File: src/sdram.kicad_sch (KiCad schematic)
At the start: 8 parts, among them U1 ECP5U_12_CABGA256, U10 W9825G6KH-6

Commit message: Rev 2
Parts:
- C30, C32: LCSC Part (none) -> C19702
- C31, C33, C34, C35: LCSC Part (none) -> C1525
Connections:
- net LED1: now reaches U1.C13 (PT60B/-)
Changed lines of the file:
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@@
 		)
 	)
+	(global_label "LED1"
+		(shape input)
+		(at 214.63 115.57 180)
+		(effects
+			(font
+				(size 1.27 1.27)
+			)
+			(justify right)
+		)
+		(property "Intersheetrefs" "${INTERSHEET_REFS}"
+			(at 214.63 115.57 0)
+			(effects
+				(font
+					(size 1.27 1.27)
+					(thickness 0.254)
+					(bold yes)
+				)
+				(hide yes)
+			)
+		)
+	)
 	(global_label "SDRAM_A1"
 		(shape input)
@@
 			)
 		)
-		(property "LCSC Part" ""
+		(property "LCSC Part" "C19702"
 			(at 222.25 36.83 0)
 			(effects
@@
 			)
 		)
-		(property "LCSC Part" ""
+		(property "LCSC Part" "C1525"
 			(at 133.35 35.56 0)
 			(effects
@@
 			)
 		)
-		(property "LCSC Part" ""
+		(property "LCSC Part" "C1525"
 			(at 48.26 113.03 0)
 			(effects
@@
 			)
 		)
-		(property "LCSC Part" ""
+		(property "LCSC Part" "C1525"
 			(at 233.68 36.83 0)
 			(effects
@@
 			)
 		)
-		(property "LCSC Part" ""
+		(property "LCSC Part" "C1525"
 			(at 246.38 36.83 0)
 			(effects
@@
 			)
 		)
-		(property "LCSC Part" ""
+		(property "LCSC Part" "C19702"
 			(at 121.92 35.56 0)
 			(effects

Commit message: Tidy project
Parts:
- C30, C32: JLCPCB Part # (none) -> C19702; LCSC Part C19702 -> (none)
- C31, C33, C34, C35: JLCPCB Part # (none) -> C1525; LCSC Part C1525 -> (none)
- U1: JLCPCB Part # (none) -> C1521614; LCSC Part C1521614 -> (none)
- U10: JLCPCB Part # (none) -> C62246; LCSC Part C62246 -> (none)
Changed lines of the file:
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@@
 			)
 		)
-		(property "LCSC Part" "C19702"
+		(property "JLCPCB Part #" "C19702"
 			(at 222.25 36.83 0)
 			(effects
@@
 					(size 1.27 1.27)
 				)
-				(hide yes)
 			)
 		)
@@
 			)
 		)
-		(property "LCSC Part" " C1521614"
+		(property "JLCPCB Part #" " C1521614"
 			(at 236.22 85.09 0)
 			(effects
@@
 					(size 1.27 1.27)
 				)
-				(hide yes)
 			)
 		)
@@
 			)
 		)
-		(property "LCSC Part" " C1521614"
+		(property "JLCPCB Part #" " C1521614"
 			(at 63.5 162.56 0)
 			(effects
@@
 					(size 1.27 1.27)
 				)
-				(hide yes)
 			)
 		)
@@
 			)
 		)
-		(property "LCSC Part" " C62246"
+		(property "JLCPCB Part #" " C62246"
 			(at 49.53 53.34 0)
 			(effects
@@
 					(size 1.27 1.27)
 				)
-				(hide yes)
 			)
 		)
@@
 			)
 		)
-		(property "LCSC Part" "C1525"
+		(property "JLCPCB Part #" "C1525"
 			(at 133.35 35.56 0)
 			(effects
@@
 					(size 1.27 1.27)
 				)
-				(hide yes)
 			)
 		)
@@
 			)
 		)
-		(property "LCSC Part" "C1525"
+		(property "JLCPCB Part #" "C1525"
 			(at 48.26 113.03 0)
 			(effects
@@
 					(size 1.27 1.27)
 				)
-				(hide yes)
 			)
 		)
@@
 			)
 		)
-		(property "LCSC Part" "C1525"
+		(property "JLCPCB Part #" "C1525"
 			(at 233.68 36.83 0)
 			(effects
@@
 					(size 1.27 1.27)
 				)
-				(hide yes)
 			)
 		)
@@
 			)
 		)
-		(property "LCSC Part" " C1521614"
+		(property "JLCPCB Part #" " C1521614"
 			(at 135.89 85.09 0)
 			(effects
@@
 					(size 1.27 1.27)
 				)
-				(hide yes)
 			)
 		)
@@
 			)
 		)
-		(property "LCSC Part" "C1525"
+		(property "JLCPCB Part #" "C1525"
 			(at 246.38 36.83 0)
 			(effects
@@
 					(size 1.27 1.27)
 				)
-				(hide yes)
 			)
 		)
@@
 			)
 		)
-		(property "LCSC Part" "C19702"
+		(property "JLCPCB Part #" "C19702"
 			(at 121.92 35.56 0)
 			(effects
@@
 					(size 1.27 1.27)
 				)
-				(hide yes)
-			)
-		)
+			)
+		)

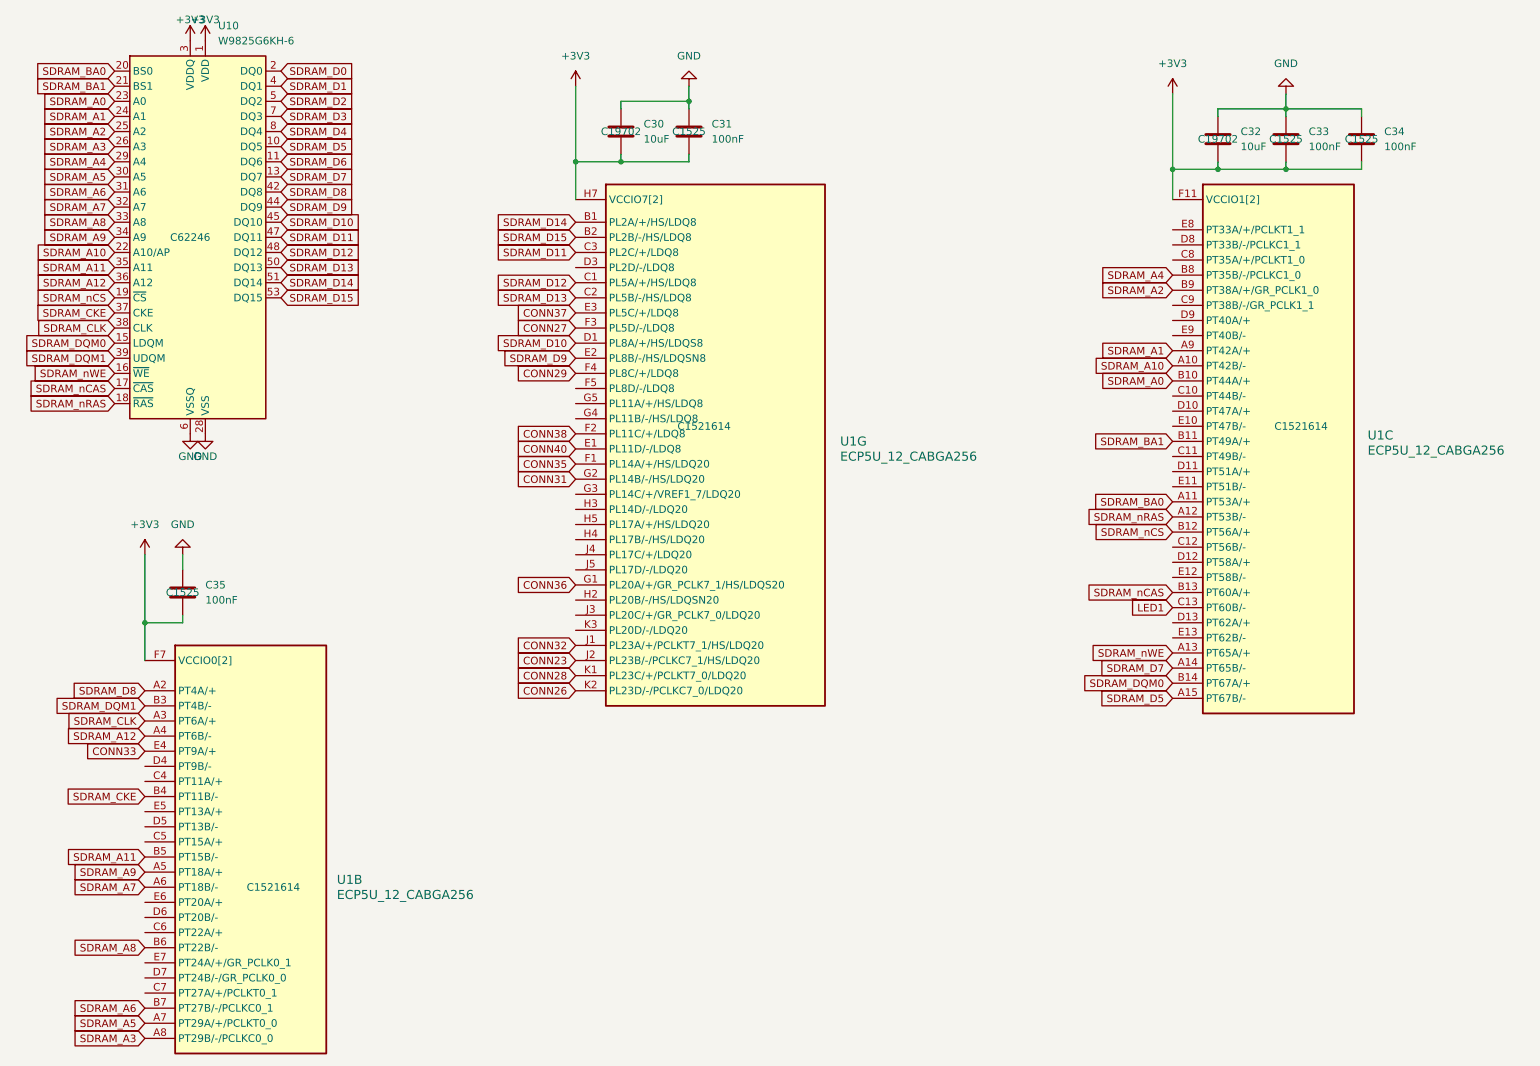
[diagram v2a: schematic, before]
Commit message: Add test points
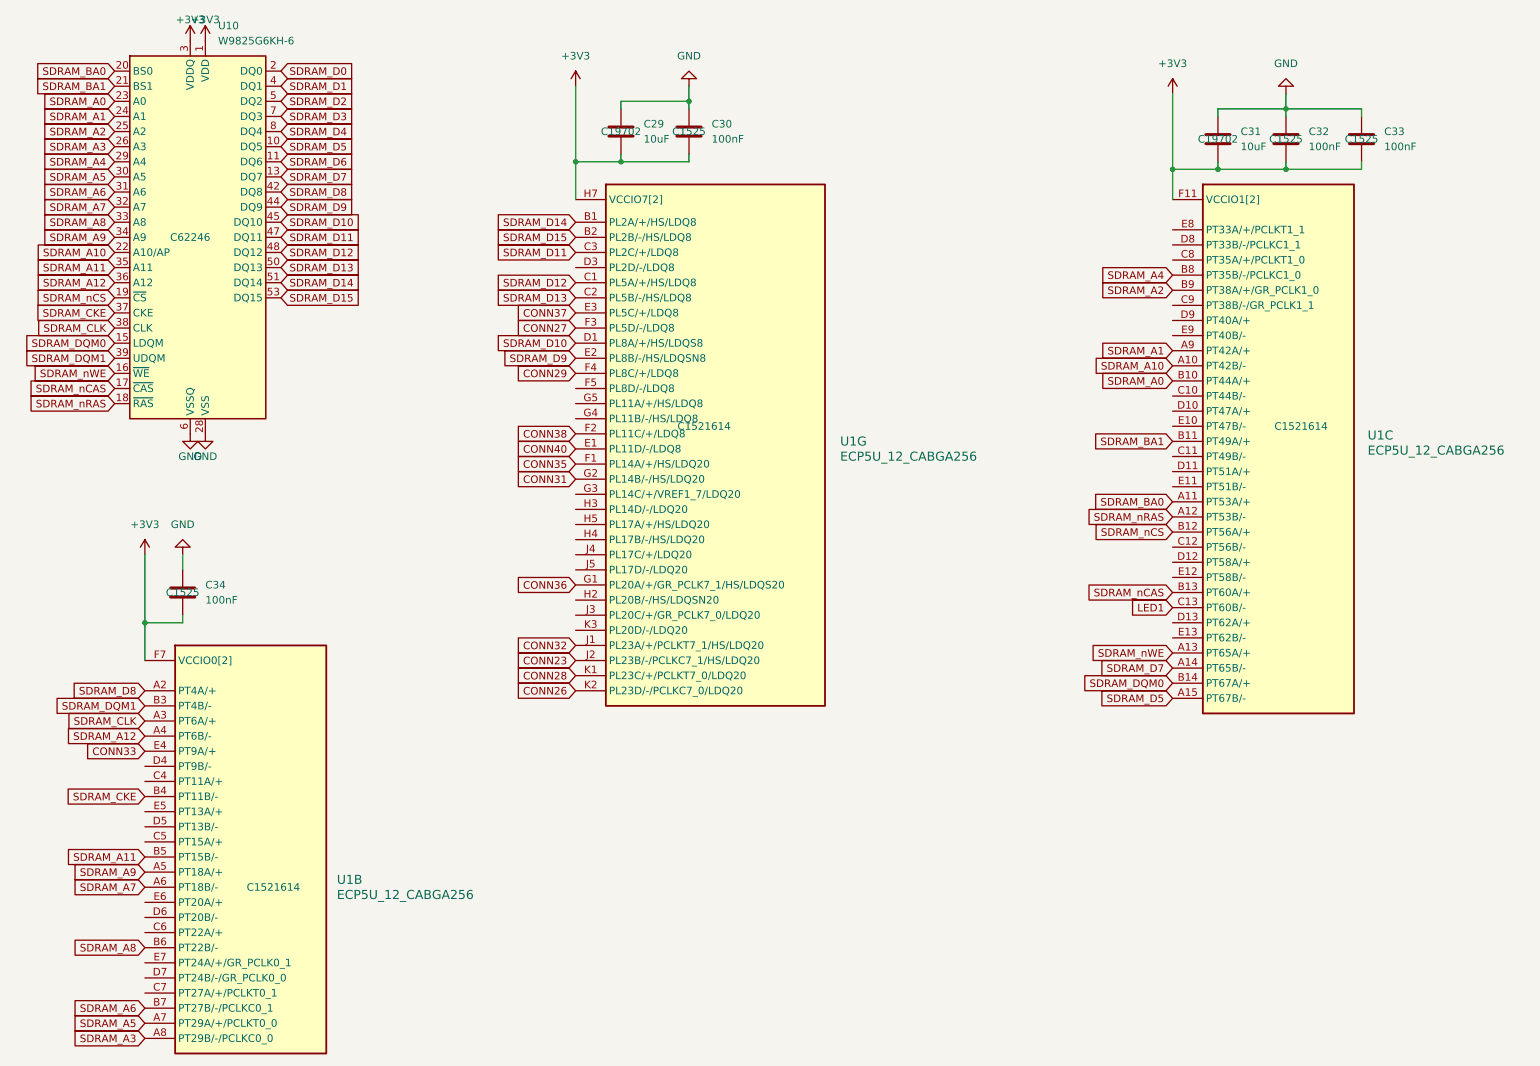
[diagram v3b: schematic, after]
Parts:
- renumbered C30 to C29, C31 to C30, C32 to C31, C33 to C32, C34 to C33, C35 to C34
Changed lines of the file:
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@@
 		(on_board yes)
 		(dnp no)
-		(property "Reference" "#PWR061"
+		(property "Reference" "#PWR070"
 			(at 49.53 24.13 0)
 			(effects
@@
 			(project "anice"
 				(path "/0f1188ca-7a22-47ac-a6b4-e14ae08f1e6d/b8864f4a-1b1e-4293-9ee7-0fecc8962eec"
-					(reference "#PWR061")
+					(reference "#PWR070")
 					(unit 1)
 				)
@@
 		(on_board yes)
 		(dnp no)
-		(property "Reference" "#PWR063"
+		(property "Reference" "#PWR076"
 			(at 49.53 92.71 0)
 			(effects
@@
 			(project "anice"
 				(path "/0f1188ca-7a22-47ac-a6b4-e14ae08f1e6d/b8864f4a-1b1e-4293-9ee7-0fecc8962eec"
-					(reference "#PWR063")
+					(reference "#PWR076")
 					(unit 1)
 				)
@@
 		(dnp no)
 		(fields_autoplaced yes)
-		(property "Reference" "C32"
+		(property "Reference" "C31"
 			(at 226.06 35.5599 0)
 			(effects
@@
 			(project "anice"
 				(path "/0f1188ca-7a22-47ac-a6b4-e14ae08f1e6d/b8864f4a-1b1e-4293-9ee7-0fecc8962eec"
-					(reference "C32")
+					(reference "C31")
 					(unit 1)
 				)
@@
 		(on_board yes)
 		(dnp no)
-		(property "Reference" "#PWR064"
+		(property "Reference" "#PWR077"
 			(at 52.07 92.71 0)
 			(effects
@@
 			(project "anice"
 				(path "/0f1188ca-7a22-47ac-a6b4-e14ae08f1e6d/b8864f4a-1b1e-4293-9ee7-0fecc8962eec"
-					(reference "#PWR064")
+					(reference "#PWR077")
 					(unit 1)
 				)
@@
 		(dnp no)
 		(fields_autoplaced yes)
-		(property "Reference" "C31"
+		(property "Reference" "C30"
 			(at 137.16 34.2899 0)
 			(effects
@@
 			(project "anice"
 				(path "/0f1188ca-7a22-47ac-a6b4-e14ae08f1e6d/b8864f4a-1b1e-4293-9ee7-0fecc8962eec"
-					(reference "C31")
+					(reference "C30")
 					(unit 1)
 				)
@@
 		(dnp no)
 		(fields_autoplaced yes)
-		(property "Reference" "#PWR083"
+		(property "Reference" "#PWR072"
 			(at 114.3 31.75 0)
 			(effects
@@
 			(project "anice"
 				(path "/0f1188ca-7a22-47ac-a6b4-e14ae08f1e6d/b8864f4a-1b1e-4293-9ee7-0fecc8962eec"
-					(reference "#PWR083")
+					(reference "#PWR072")
 					(unit 1)
 				)
@@
 		(dnp no)
 		(fields_autoplaced yes)
-		(property "Reference" "C35"
+		(property "Reference" "C34"
 			(at 52.07 111.7599 0)
 			(effects
@@
 			(project "anice"
 				(path "/0f1188ca-7a22-47ac-a6b4-e14ae08f1e6d/b8864f4a-1b1e-4293-9ee7-0fecc8962eec"
-					(reference "C35")
+					(reference "C34")
 					(unit 1)
 				)
@@
 		(dnp no)
 		(fields_autoplaced yes)
-		(property "Reference" "C33"
+		(property "Reference" "C32"
 			(at 237.49 35.5599 0)
 			(effects
@@
 			(project "anice"
 				(path "/0f1188ca-7a22-47ac-a6b4-e14ae08f1e6d/b8864f4a-1b1e-4293-9ee7-0fecc8962eec"
-					(reference "C33")
+					(reference "C32")
 					(unit 1)
 				)
@@
 		(dnp no)
 		(fields_autoplaced yes)
-		(property "Reference" "#PWR085"
+		(property "Reference" "#PWR074"
 			(at 214.63 33.02 0)
 			(effects
@@
 			(project "anice"
 				(path "/0f1188ca-7a22-47ac-a6b4-e14ae08f1e6d/b8864f4a-1b1e-4293-9ee7-0fecc8962eec"
-					(reference "#PWR085")
+					(reference "#PWR074")
 					(unit 1)
 				)
@@
 		(dnp no)
 		(fields_autoplaced yes)
-		(property "Reference" "#PWR088"
+		(property "Reference" "#PWR079"
 			(at 48.26 100.33 0)
 			(effects
@@
 			(project "anice"
 				(path "/0f1188ca-7a22-47ac-a6b4-e14ae08f1e6d/b8864f4a-1b1e-4293-9ee7-0fecc8962eec"
-					(reference "#PWR088")
+					(reference "#PWR079")
 					(unit 1)
 				)
@@
 		(dnp no)
 		(fields_autoplaced yes)
-		(property "Reference" "#PWR087"
+		(property "Reference" "#PWR078"
 			(at 41.91 110.49 0)
 			(effects
@@
 			(project "anice"
 				(path "/0f1188ca-7a22-47ac-a6b4-e14ae08f1e6d/b8864f4a-1b1e-4293-9ee7-0fecc8962eec"
-					(reference "#PWR087")
+					(reference "#PWR078")
 					(unit 1)
 				)
@@
 		(dnp no)
 		(fields_autoplaced yes)
-		(property "Reference" "C34"
+		(property "Reference" "C33"
 			(at 250.19 35.5599 0)
 			(effects
@@
 			(project "anice"
 				(path "/0f1188ca-7a22-47ac-a6b4-e14ae08f1e6d/b8864f4a-1b1e-4293-9ee7-0fecc8962eec"
-					(reference "C34")
+					(reference "C33")
 					(unit 1)
 				)
@@
 		(dnp no)
 		(fields_autoplaced yes)
-		(property "Reference" "#PWR084"
+		(property "Reference" "#PWR073"
 			(at 133.35 21.59 0)
 			(effects
@@
 			(project "anice"
 				(path "/0f1188ca-7a22-47ac-a6b4-e14ae08f1e6d/b8864f4a-1b1e-4293-9ee7-0fecc8962eec"
-					(reference "#PWR084")
+					(reference "#PWR073")
 					(unit 1)
 				)
@@
 		(on_board yes)
 		(dnp no)
-		(property "Reference" "#PWR062"
+		(property "Reference" "#PWR071"
 			(at 52.07 24.13 0)
 			(effects
@@
 			(project "anice"
 				(path "/0f1188ca-7a22-47ac-a6b4-e14ae08f1e6d/b8864f4a-1b1e-4293-9ee7-0fecc8962eec"
-					(reference "#PWR062")
+					(reference "#PWR071")
 					(unit 1)
 				)
@@
 		(dnp no)
 		(fields_autoplaced yes)
-		(property "Reference" "#PWR086"
+		(property "Reference" "#PWR075"
 			(at 233.68 22.86 0)
 			(effects
@@
 			(project "anice"
 				(path "/0f1188ca-7a22-47ac-a6b4-e14ae08f1e6d/b8864f4a-1b1e-4293-9ee7-0fecc8962eec"
-					(reference "#PWR086")
+					(reference "#PWR075")
 					(unit 1)
 				)
@@
 		(dnp no)
 		(fields_autoplaced yes)
-		(property "Reference" "C30"
+		(property "Reference" "C29"
 			(at 125.73 34.2899 0)
 			(effects
@@
 			(project "anice"
 				(path "/0f1188ca-7a22-47ac-a6b4-e14ae08f1e6d/b8864f4a-1b1e-4293-9ee7-0fecc8962eec"
-					(reference "C30")
+					(reference "C29")
 					(unit 1)
 				)
